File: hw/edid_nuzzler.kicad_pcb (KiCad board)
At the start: 2 copper layers, 49 x 32 mm, 49 parts, among them J1 HDMI_A, J2 HDMI_A, J4 USB_C_Receptacle_USB2.0_16P, J5 Prog, Q1 BSS84AK, SW1 SW_Push, U1 74LVC1G3157, U2 74LVC1G3157, U3 CH340N, U4 CH32V003AxMx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

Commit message: Corase layout
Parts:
- TP1, TP10, TP11, TP12, TP13, TP14, TP4, TP6, TP7, TP8, TP9: value ~ -> pad; footprint nuzzler:Pin_tight -> TestPoint:TestPoint_Pad_D1.0mm
- TP2, TP3, TP5: footprint nuzzler:Pin_tight -> TestPoint:TestPoint_THTPad_D1.5mm_Drill0.7mm
- moved R11 24.5 mm to (183.6, 53.3)
- moved R10 24.1 mm to (196.6, 91.0)
- moved U1 16.6 mm to (193.4, 87.7), turned to 180 degrees
- moved R3 15.9 mm to (187.8, 90.4)
- moved R9 15.8 mm to (187.1, 87.7)
- moved R13 15.6 mm to (187.8, 91.9)
- moved R4 12.6 mm to (192.7, 64.5)
- moved R1 12.1 mm to (196.6, 84.3), turned to 90 degrees
- moved R7 11.9 mm to (188.7, 87.7), turned to -90 degrees
- moved U2 11.5 mm to (193.4, 84.3), turned to 180 degrees
- moved R2 10.7 mm to (196.6, 87.6), turned to 90 degrees
- moved R6 10.6 mm to (188.7, 84.3)
- moved C5 10.0 mm to (190.2, 87.6), turned to -90 degrees
- moved R12 8.39 mm to (203.6, 66.5), turned to -90 degrees
- moved C3 8.31 mm to (195.4, 63.6), turned to 0 degrees
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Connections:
- net Net-(J1-CK+) renamed /CK+
- net Net-(J1-CK-) renamed /CK-
- net Net-(J1-D0+) renamed /D0+
- net Net-(J1-D0-) renamed /D0-
- net Net-(J1-D1+) renamed /D1+
- net Net-(J1-D1-) renamed /D1-
- net Net-(J1-D2+) renamed /D2+
- net Net-(J1-D2-) renamed /D2-
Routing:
- net /CK-: track 0.00 -> 62.8 mm
- net /CK+: track 0.00 -> 61.2 mm
- net /D0-: track 0.00 -> 51.6 mm
- net /D0+: track 0.00 -> 50.2 mm
- net /D2-: track 0.00 -> 42.8 mm
- net /D1-: track 0.00 -> 42.4 mm
- net /D2+: track 0.00 -> 41.4 mm
- net /D1+: track 0.00 -> 41.0 mm
- net GND: vias 0 -> 1
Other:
- outline, holes or cut-outs redrawn
- copper layers 2 -> 4

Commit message: Hopefully better high speed layout
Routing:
- net /CK-: track 62.8 -> 60.6 mm
- net /CK+: track 61.2 -> 59.5 mm
- net /D0-: track 51.6 -> 50.0 mm
- net /D0+: track 50.2 -> 48.9 mm
- net /D2-: track 42.8 -> 41.9 mm
- net /D2+: track 41.4 -> 40.8 mm
- net /D1-: track 42.4 -> 41.9 mm

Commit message: PCB wip
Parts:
- moved R10 0.12 mm to (196.6, 91.1)
- moved R1 0.10 mm to (196.6, 84.2)
- moved R6 0.09 mm to (188.8, 84.3)
- moved R2 0.07 mm to (196.6, 87.7)
- moved C7 0.05 mm to (190.2, 91.0)
- turned R13 to 180 degrees
- turned R3 to 180 degrees
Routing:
- net GND: track 0.00 -> 34.3 mm, vias 1 -> 24
- net Net-(J2-SDA): track 0.00 -> 28.5 mm, vias 0 -> 2
- net Net-(J2-SCL): track 0.00 -> 23.3 mm, vias 0 -> 2
- net +5V: track 0.00 -> 18.4 mm, vias 0 -> 10
- net Net-(J1-SDA): track 0.00 -> 14.6 mm, vias 0 -> 1
- net Net-(R13-Pad1): track 0.00 -> 11.2 mm
- net Net-(J1-SCL): track 0.00 -> 7.89 mm, vias 0 -> 2
- net Net-(J1-HPD): track 0.00 -> 7.18 mm, vias 0 -> 2
- net Net-(U4-PD4): track 0.00 -> 5.00 mm
- net Net-(J1-CEC): track 0.00 -> 2.55 mm, vias 0 -> 1
- net Net-(J5-Pin_3): track 0.00 -> 2.55 mm, vias 0 -> 1
- net Net-(J1-UTILITY): track 0.00 -> 2.52 mm, vias 0 -> 1
- net Net-(U4-PC6): track 0.00 -> 2.49 mm, vias 0 -> 1
- net Net-(J2-HPD): track 0.00 -> 2.47 mm, vias 0 -> 2
- net Net-(U4-PD7): track 0.00 -> 2.36 mm, vias 0 -> 1
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- added copper zone on B.Cu, net +5V
- added copper zone on In1.Cu, net GND

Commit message: Rough idea about routing
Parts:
- removed C6: 1u, Capacitor_SMD:C_0603_1608Metric_Pad1.08x0.95mm_HandSolder
- removed J5: Prog, nuzzler:PinHeader_1x03_P2.54mm_Vertical_Tight
- removed R11: 5k1, Resistor_SMD:R_0603_1608Metric_Pad0.98x0.95mm_HandSolder
- removed TP2, TP3, TP5: ~, TestPoint:TestPoint_THTPad_D1.5mm_Drill0.7mm
- removed TP8: pad, TestPoint:TestPoint_Pad_D1.0mm
- removed U6: ZD24C16A-STGMT, Package_TO_SOT_SMD:SOT-23-5
- added J3: Conn_02x03_Counter_Clockwise, Connector_PinHeader_2.54mm:PinHeader_2x03_P2.54mm_Vertical, F.Cu at (164.1, 64.8)
- moved TP1 24.4 mm to (202.4, 66.6)
- moved C3 9.10 mm to (199.5, 71.8), turned to 180 degrees
- moved C8 7.12 mm to (199.5, 64.8), turned to 180 degrees
- moved TP4 6.94 mm to (164.3, 72.8)
- moved TP7 3.99 mm to (166.4, 74.9)
- moved TP6 3.69 mm to (166.4, 72.8)
- moved TP9 2.79 mm to (164.3, 74.9)
- moved D2 2.75 mm to (186.9, 73.2), turned to 180 degrees
- moved R5 1.95 mm to (192.6, 70.1)
- moved C2 1.29 mm to (186.9, 71.2), turned to 0 degrees
- moved R4 1.21 mm to (193.8, 64.8), turned to 0 degrees
- moved U3 1.15 mm to (197.4, 68.3), turned to 0 degrees
- moved C1 1.09 mm to (177.7, 65.7), turned to -90 degrees
- moved D1 0.63 mm to (204.2, 69.9)
- moved R12 0.63 mm to (204.2, 66.5)
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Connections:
- net Net-(U3-UD+) renamed /UD+
- net Net-(U3-UD-) renamed /UD-
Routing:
- net Net-(J1-SCL): track 7.89 -> 67.0 mm, vias 2 -> 4
- net Net-(D2-K): track 0.00 -> 57.4 mm
- net Net-(U4-PC3): track 0.54 -> 51.0 mm, vias 1 -> 2
- net Net-(J1-CEC): track 2.55 -> 48.5 mm, vias 1 -> 2
- net Net-(J1-HPD): track 7.18 -> 52.7 mm
- net Net-(J1-UTILITY): track 2.52 -> 46.2 mm, vias 1 -> 2
- net Net-(U4-PC4): track 0.89 -> 43.2 mm, vias 1 -> 2
- net Net-(J1-SDA): track 14.6 -> 55.1 mm, vias 1 -> 3
- net Net-(U4-PC6): track 2.49 -> 42.1 mm, vias 1 -> 2
- net Net-(J3-Pin_3): track 2.55 -> 42.1 mm, vias 1 -> 2
- net Net-(U4-PD4): track 5.00 -> 41.4 mm, vias 0 -> 2
- net Net-(U4-PA1): track 0.79 -> 34.8 mm, vias 1 -> 2
- net Net-(D1-K): track 0.00 -> 33.1 mm, vias 0 -> 2
- net Net-(U4-PD7): track 2.36 -> 33.4 mm, vias 1 -> 2
- net Net-(U3-RXD): track 0.00 -> 27.2 mm, vias 0 -> 2
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
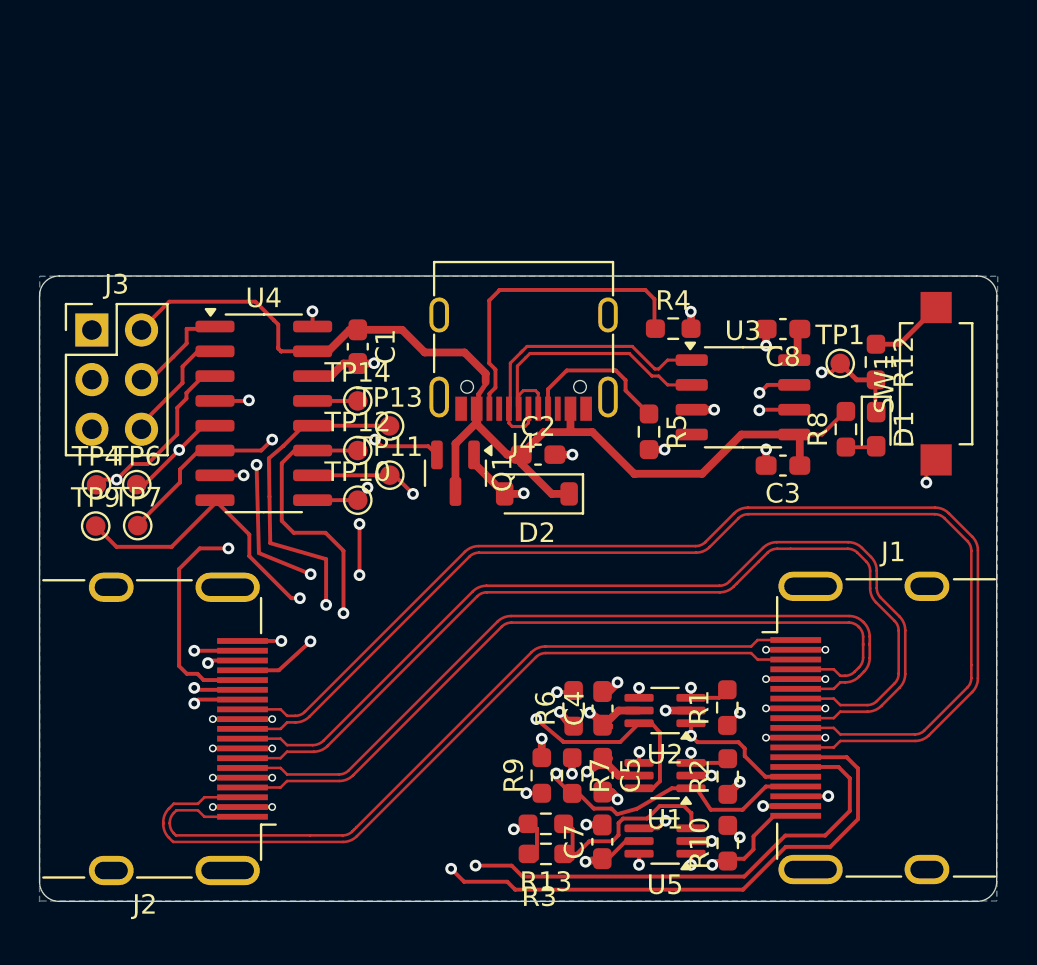
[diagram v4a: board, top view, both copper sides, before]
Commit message: trace cleanup
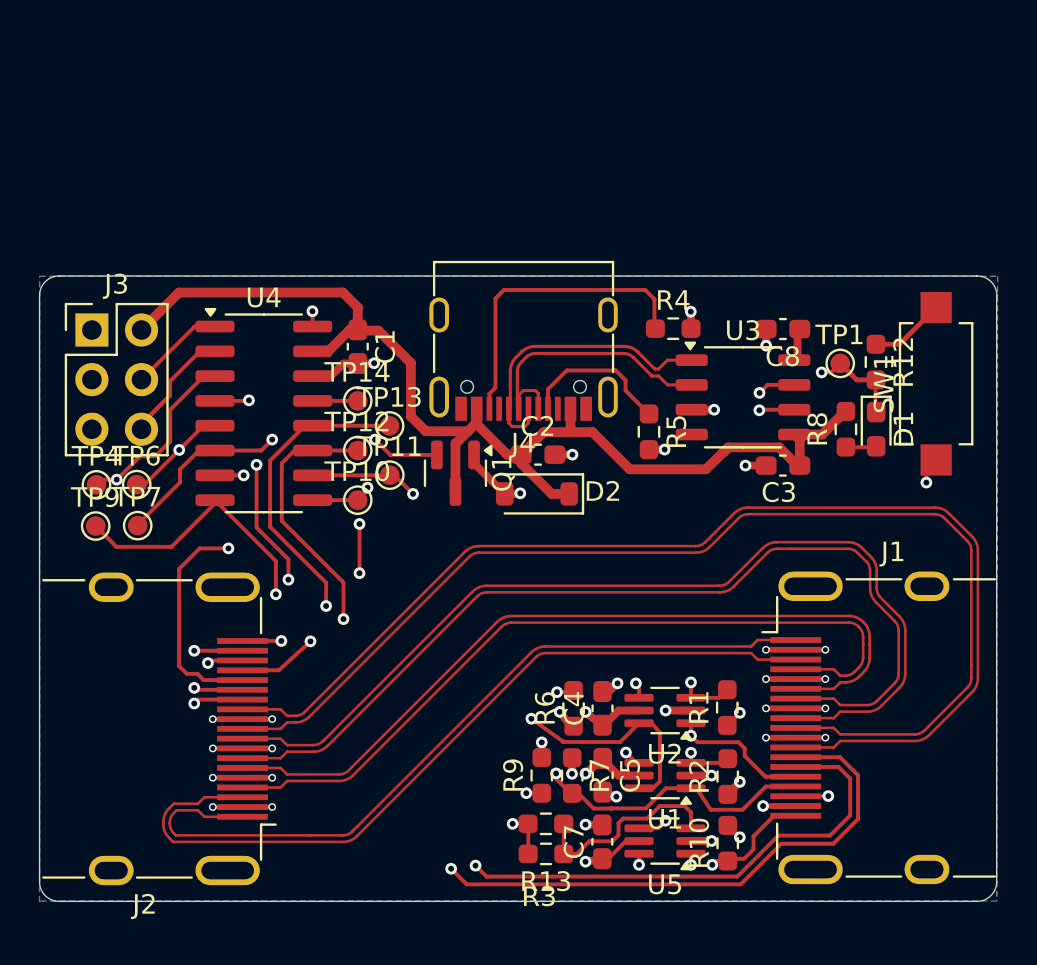
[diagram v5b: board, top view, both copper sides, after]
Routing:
- net Net-(J2-SDA): track 32.5 -> 27.7 mm
- net Net-(U4-PD7): track 33.4 -> 29.8 mm
- net Net-(U4-PA1): track 34.8 -> 31.3 mm
- net Net-(D2-K): track 57.4 -> 60.6 mm
- net Net-(U4-PC6): track 42.1 -> 44.6 mm
- net Net-(J1-SCL): track 67.0 -> 69.3 mm
- net +5V: track 23.2 -> 21.9 mm
- net Net-(U4-PC3): track 51.0 -> 49.9 mm
- net Net-(J1-CEC): track 48.5 -> 47.6 mm
- net Net-(J1-SDA): track 55.1 -> 54.2 mm
- net Net-(U4-PD4): track 41.4 -> 40.8 mm

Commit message: Mostly done
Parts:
- moved Q1 0.14 mm to (182.7, 72.3)
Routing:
- net GND: track 44.0 -> 48.8 mm
- net Net-(U3-TXD): track 26.8 -> 26.0 mm
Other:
- board text added: "Camp++"
- board text added: "Notices EDID OwO whats this?"

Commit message: v1.0 HW as sent to fab
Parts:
- moved J1 0.25 mm to (203.2, 85.3)
- moved J2 0.25 mm to (168.8, 85.3)
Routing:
- net GND: track 48.8 -> 51.0 mm
- net Net-(D1-K): track 33.1 -> 35.2 mm
- net Net-(J4-CC2): track 15.8 -> 14.4 mm
- net Net-(D2-K): track 60.6 -> 59.7 mm
- net Net-(J1-SDA): track 54.2 -> 53.7 mm
